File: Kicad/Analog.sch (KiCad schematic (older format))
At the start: 75 parts, among them J2 Conn_01x02, J3 Conn_01x02, J6 Conn_01x01, J7 Conn_01x01, Q1 IRFP150, Q2 BC557, Q3 IRFP150, Q4 BC547, Q5 BC547, U1 LM393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

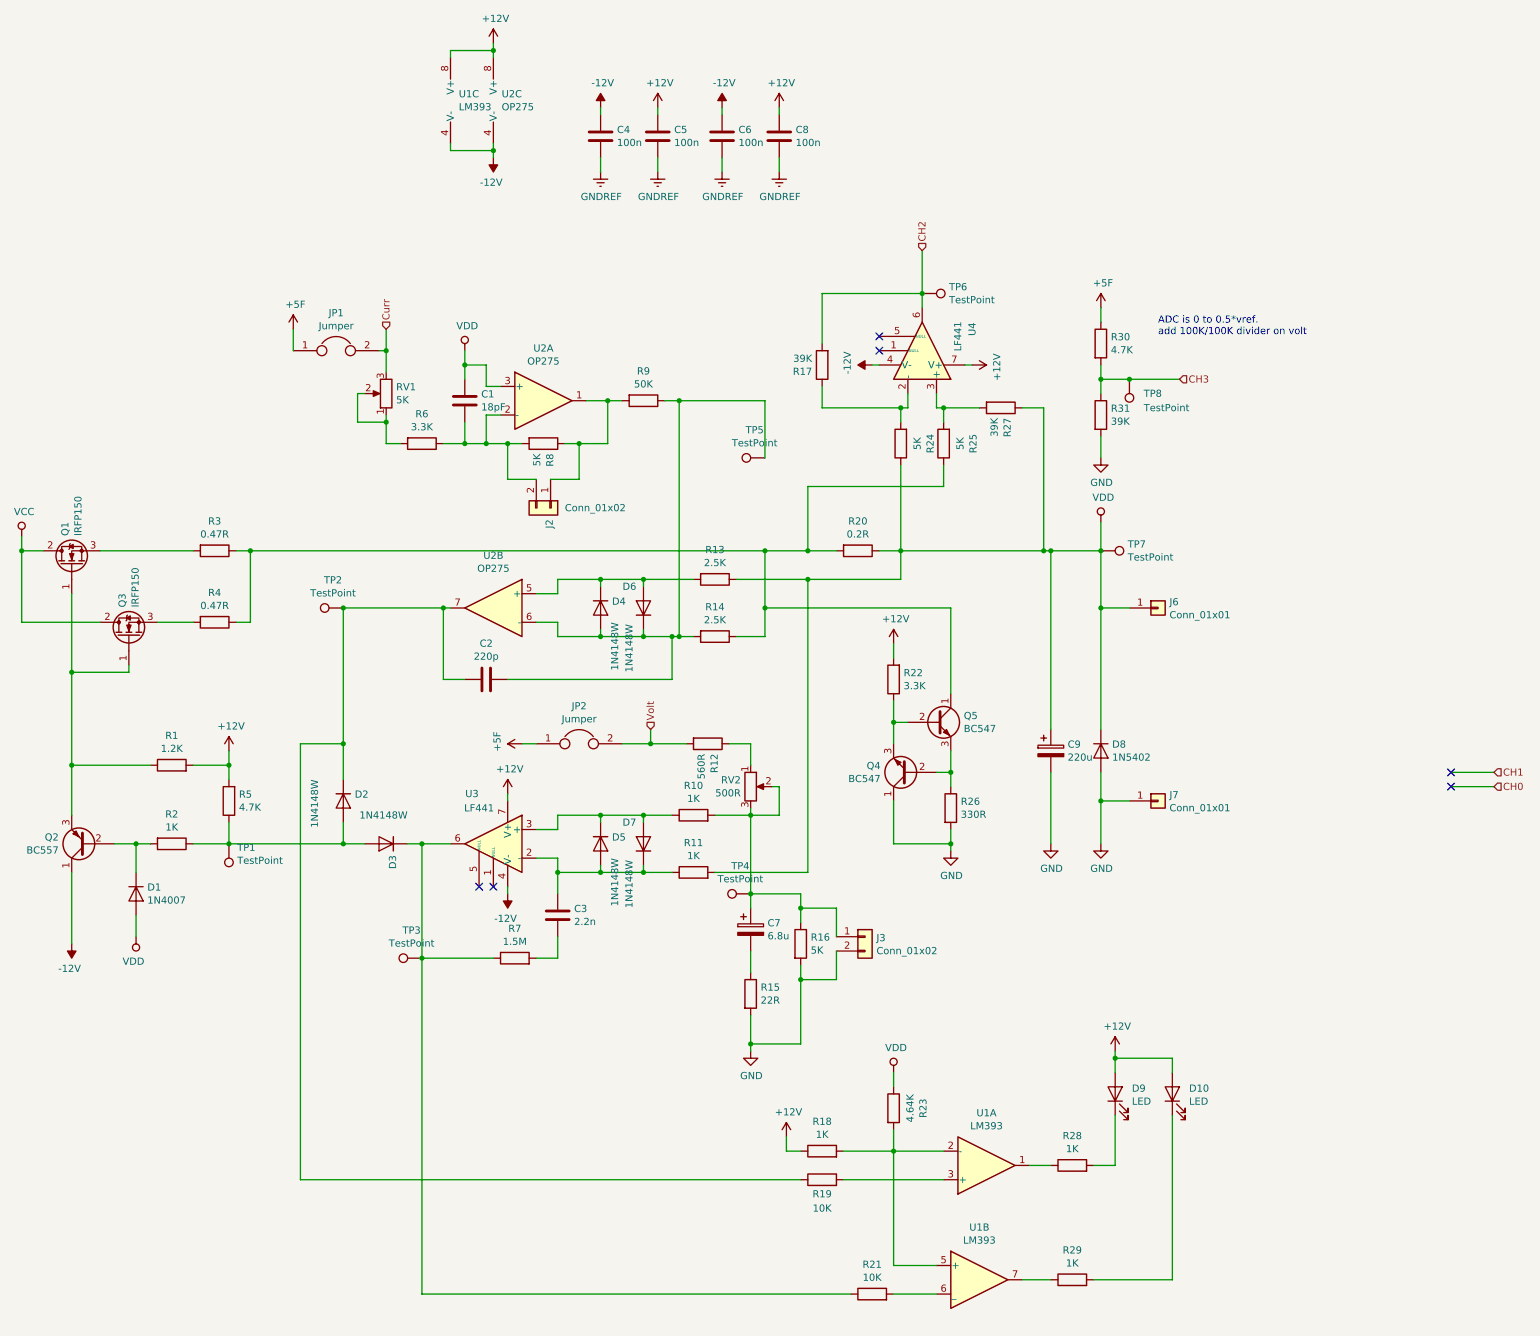
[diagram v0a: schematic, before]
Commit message: fixed bugs in PCB, added frontpanel, added SW for frontpanel
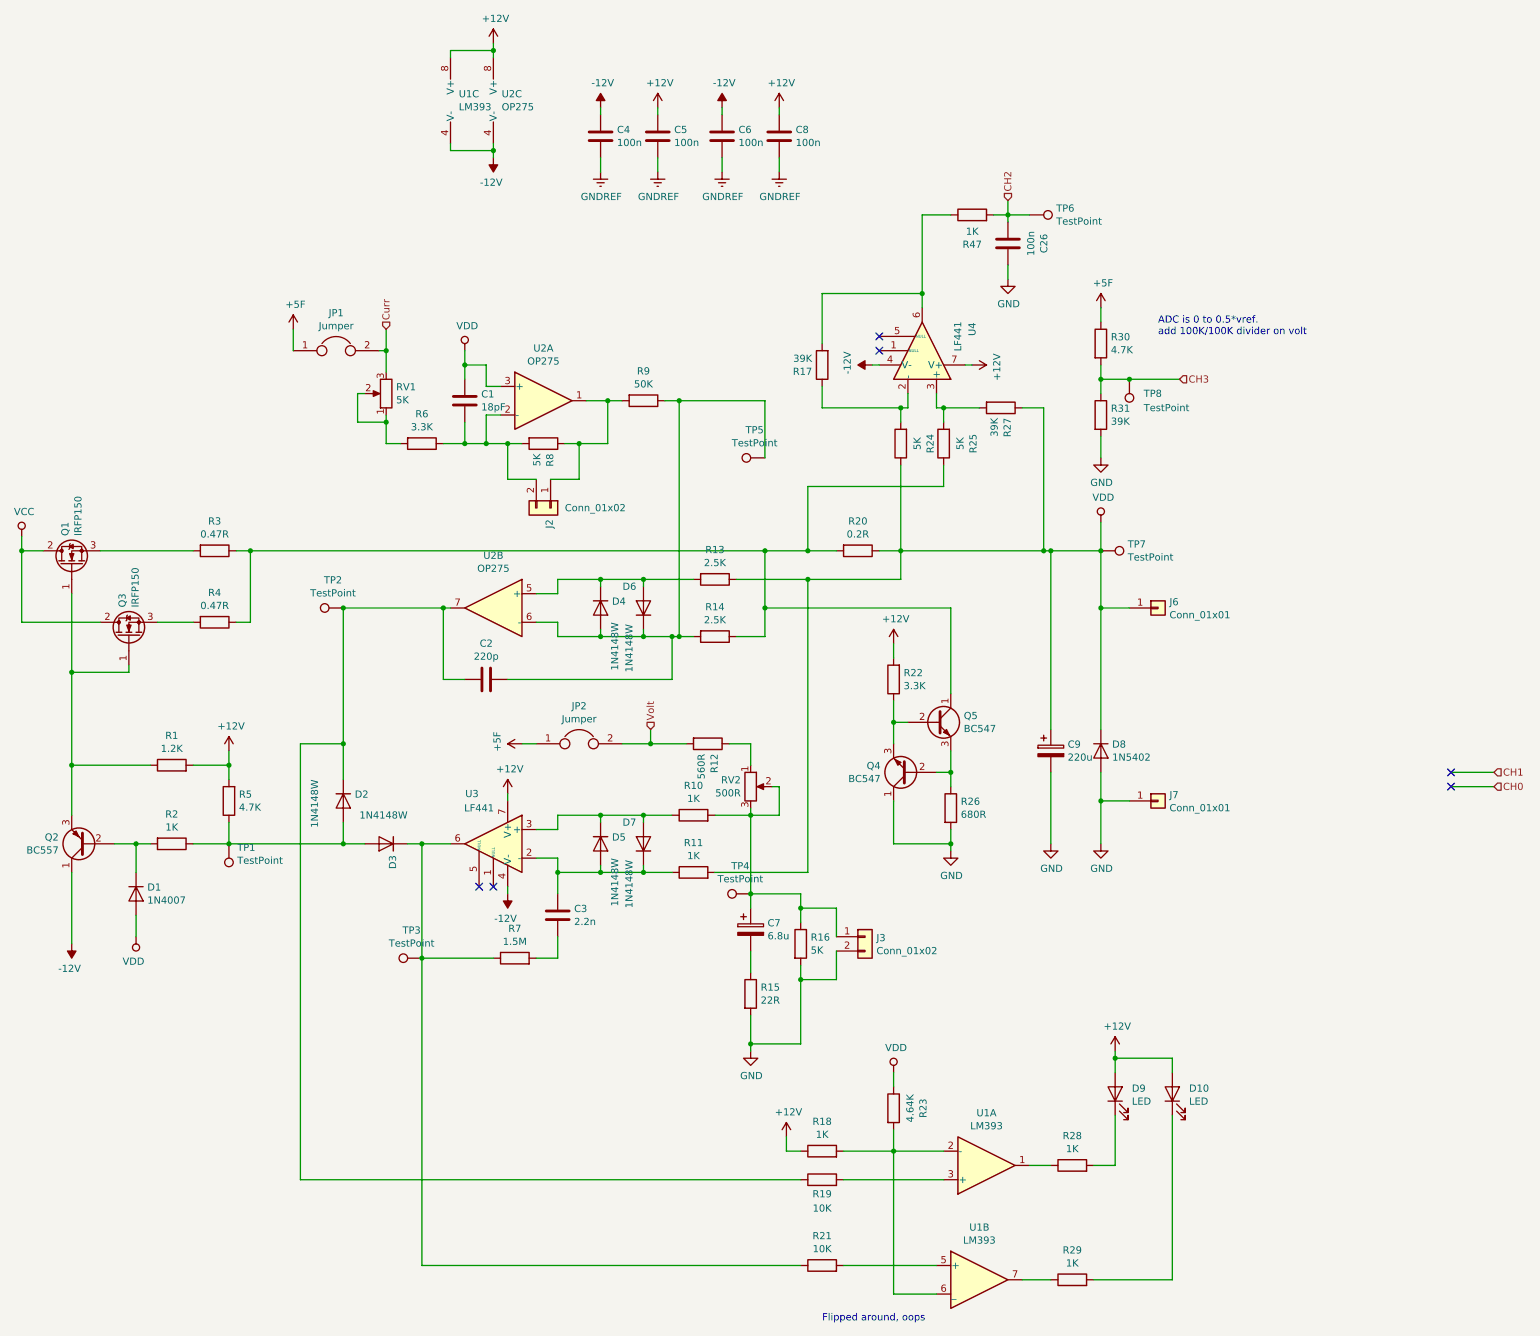
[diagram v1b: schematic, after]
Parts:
- added C26: 100n, Capacitor_SMD:C_0603_1608Metric_Pad1.05x0.95mm_HandSolder, symbol Device:C
- added R47: 1K, Resistor_SMD:R_0603_1608Metric_Pad1.05x0.95mm_HandSolder, symbol Device:R
- R26: value 330R -> 680R
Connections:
- net CH2: now also C26.2, R47.2; no longer R17.2, U4.6
- net GND: now also C26.1
- net at R18.2, R23.2, U1.2 (-): now also U1.6 (_); no longer U1.5 (+)
- net at R21.2: now also U1.5 (+); no longer U1.6 (_)
- new net: R17.2, R47.1, U4.6
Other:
- note added: "Flipped around, oops\n"
- moved on the sheet: R21, TP6
